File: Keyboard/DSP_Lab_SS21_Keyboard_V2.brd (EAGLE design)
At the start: 109 x 27 mm, 13 parts, among them J1 640455-2

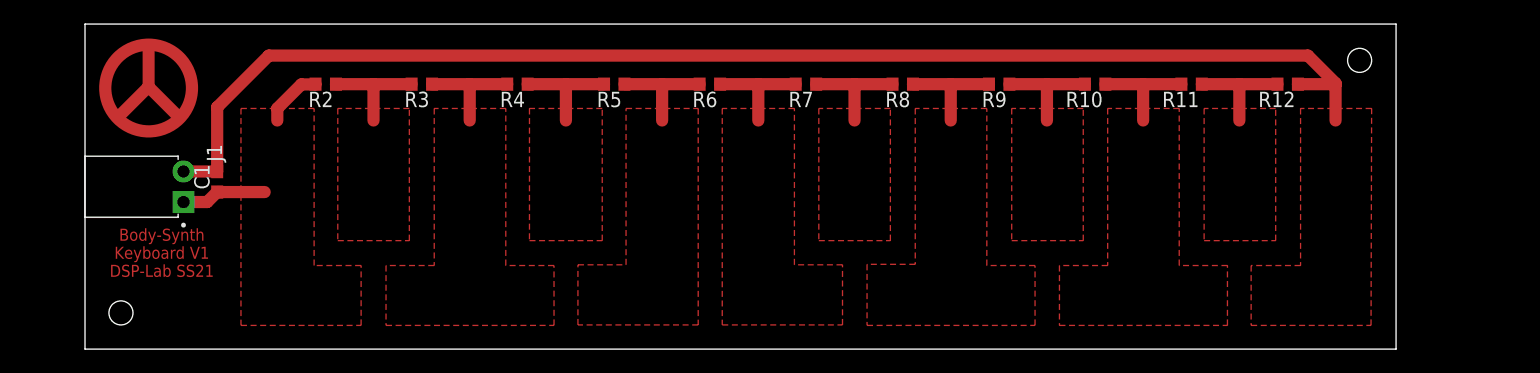
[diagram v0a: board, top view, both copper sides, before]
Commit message: # Mainboard updated
# Keyboard V2:

	# Bug fixed (lowest Pad not GND)
	# 1 more key (upper C)
	# PEACE sign corrected

# General cleanup
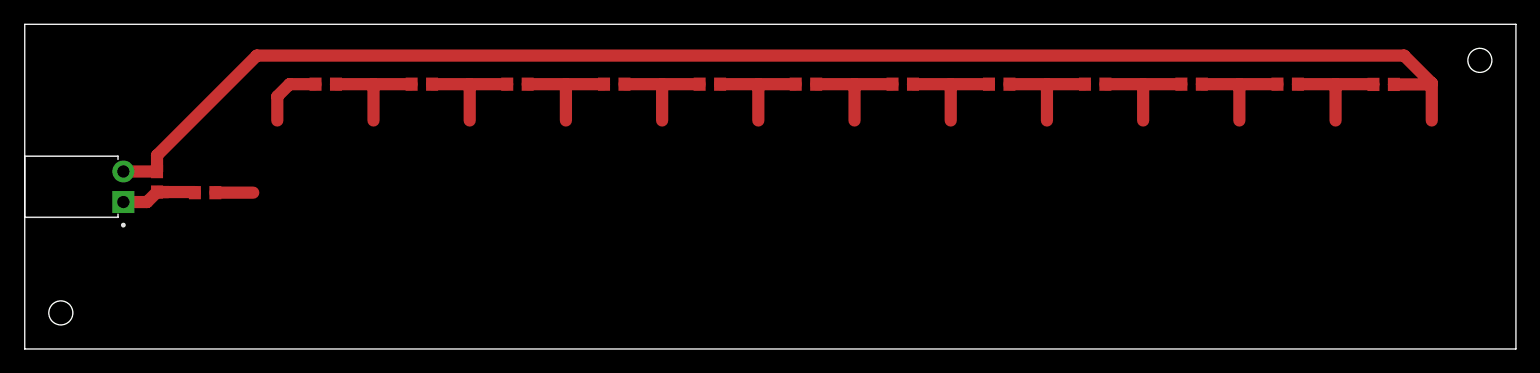
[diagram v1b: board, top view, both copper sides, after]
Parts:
- added R1, R13: 2.2k, rcl:R0603
- moved C1 5.00 mm to (6.00, 12.9)
- moved J1 5.00 mm to (3.20, 11.2)
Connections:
- new net STEP1: R1.1, R2.2
- new net STEP12: R12.1, R13.2
- net 3V3: now also R13.1; no longer R12.1
- net GND: now also R1.2; no longer R2.2
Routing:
- net 3V3: track 110.1 -> 120.8 mm
- net STEP12: track 0.00 -> 9.31 mm
- net STEP1: track 0.00 -> 8.75 mm
- net GND: track 12.2 -> 7.34 mm
- removed copper zone on layer 1, net 3V3
- removed copper zone on layer 1, net GND
- removed copper zone on layer 1, net STEP10
- removed copper zone on layer 1, net STEP11
- removed copper zone on layer 1, net STEP2
- removed copper zone on layer 1, net STEP3
- removed copper zone on layer 1, net STEP4
- removed copper zone on layer 1, net STEP5
- removed copper zone on layer 1, net STEP6
- removed copper zone on layer 1, net STEP7
- removed copper zone on layer 1, net STEP8
- removed copper zone on layer 1, net STEP9
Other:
- board size 109 x 27 mm -> 124 x 27 mm
- board text added: "Body-Synth Keyboard V2 DSP-Lab SS21"
- board text removed: "Body-Synth Keyboard V1 DSP-Lab SS21"

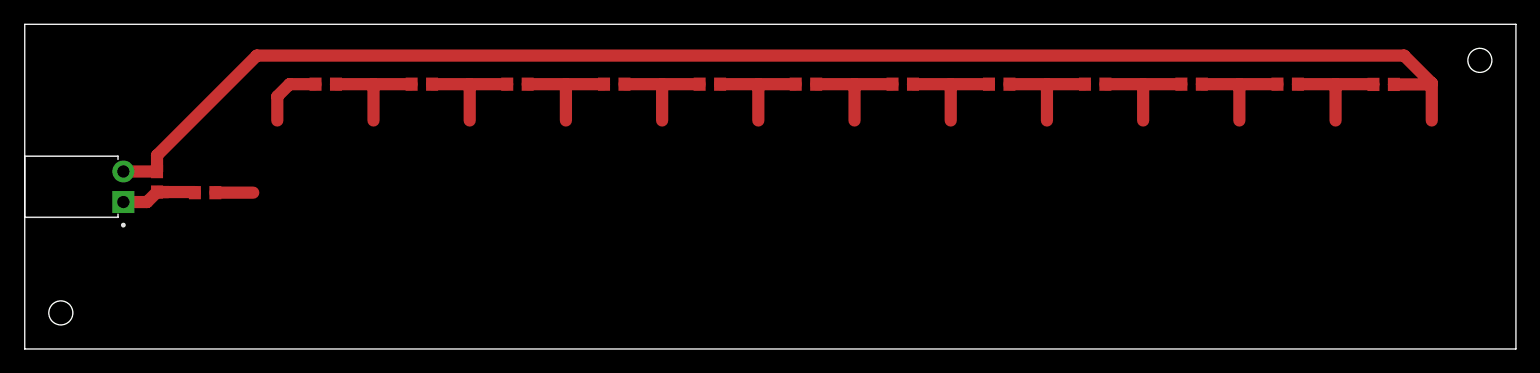
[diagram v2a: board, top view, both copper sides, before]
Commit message: Production data for ordering Mainboard, Keys, UI and EQ at JLCPCB
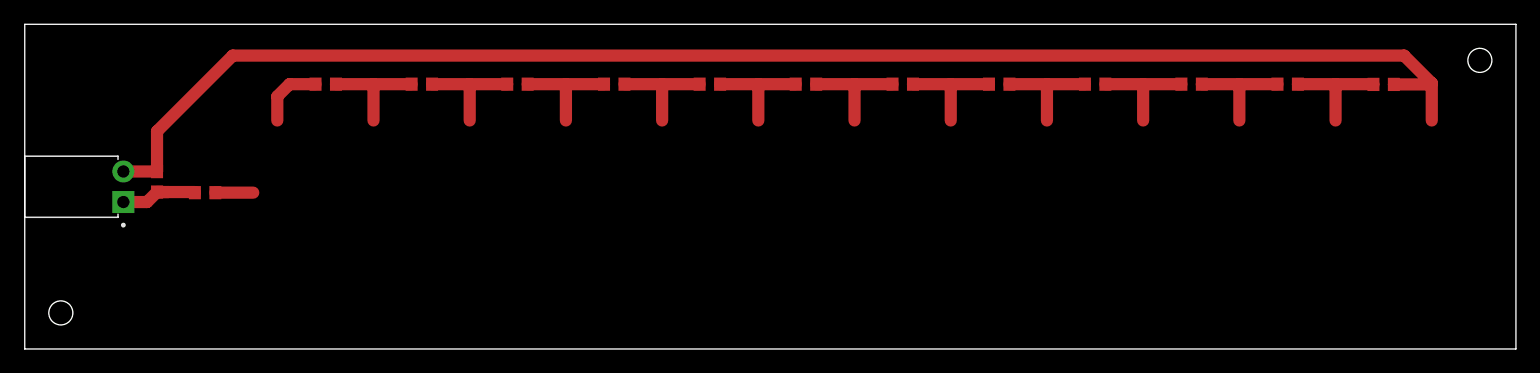
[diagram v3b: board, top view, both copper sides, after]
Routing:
- net 3V3: track 120.8 -> 122.0 mm
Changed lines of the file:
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@@
 <wire x1="112" y1="18" x2="112" y2="21.0976" width="1.016" layer="1"/>
 <wire x1="109.7" y1="23.3976" x2="112" y2="21.0976" width="1.016" layer="1"/>
-<wire x1="14.2976" y1="23.3976" x2="109.7" y2="23.3976" width="1.016" layer="1"/>
+<wire x1="12.2976" y1="23.3976" x2="109.7" y2="23.3976" width="1.016" layer="1"/>
 <contactref element="J1" pad="2"/>
 <contactref element="C1" pad="2"/>
-<wire x1="6" y1="13.75" x2="6" y2="15.1" width="1.016" layer="1"/>
-<wire x1="6" y1="15.1" x2="14.2976" y2="23.3976" width="1.016" layer="1"/>
+<wire x1="6" y1="13.75" x2="6" y2="17.1" width="1.016" layer="1"/>
+<wire x1="6" y1="17.1" x2="12.2976" y2="23.3976" width="1.016" layer="1"/>
 <wire x1="5.99" y1="13.76" x2="6" y2="13.75" width="0.8128" layer="1"/>
 <wire x1="3.2" y1="13.76" x2="5.99" y2="13.76" width="1.016" layer="1"/>
